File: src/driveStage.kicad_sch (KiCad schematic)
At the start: 73 parts, among them J4 MOD_IN, K1 DIP12-1C90-51L, Q1 BSS138, Q2 SQJA70EP-T1, SW1 204-121ST, SW2 SW_DIP_x03, U1 ADA4898-1YRDZ, U2 ADA4898-1YRDZ, U3 LTC6655BHLS8-4.096#PBF, U4 MAX5719xSD, U5 ADA4898-1YRDZ, U6 LTC6655BHMS8-4.096#PBF, U7 TL082Hx

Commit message: PCB: Correct Y169010R0000T9L Footprint - Add more space between the pin holes and resistor body
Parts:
- R24: footprint Package_TO_SOT_THT:TO-220F-4_Horizontal_TabDown -> kirdy:VPR221_Horizontal
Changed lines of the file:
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@@
       (effects (font (size 1.27 1.27)) (justify right))
     )
-    (property "Footprint" "Package_TO_SOT_THT:TO-220F-4_Horizontal_TabDown" (at 360.68 120.015 0)
+    (property "Footprint" "kirdy:VPR221_Horizontal" (at 360.68 120.015 0)
       (effects (font (size 1.27 1.27)) hide)
     )

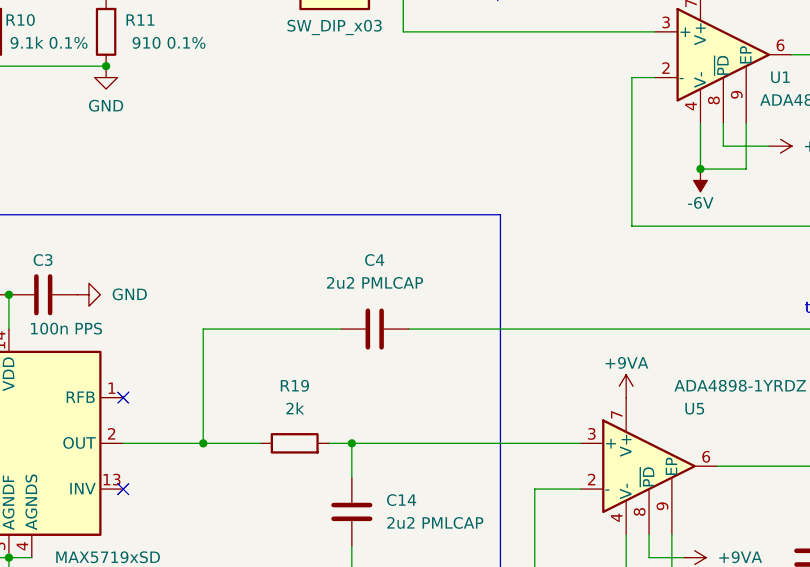
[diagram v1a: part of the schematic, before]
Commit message: sch, pcb: Add TDAC_VFB. Change 2u2 PMLCAP P/N - Connect TDAC voltage output through a RC LPF to MCU PC0(ADC123_IN10) - 2u2 PMLCAP P/N is changed to 16V version instead of 35V for lower cost
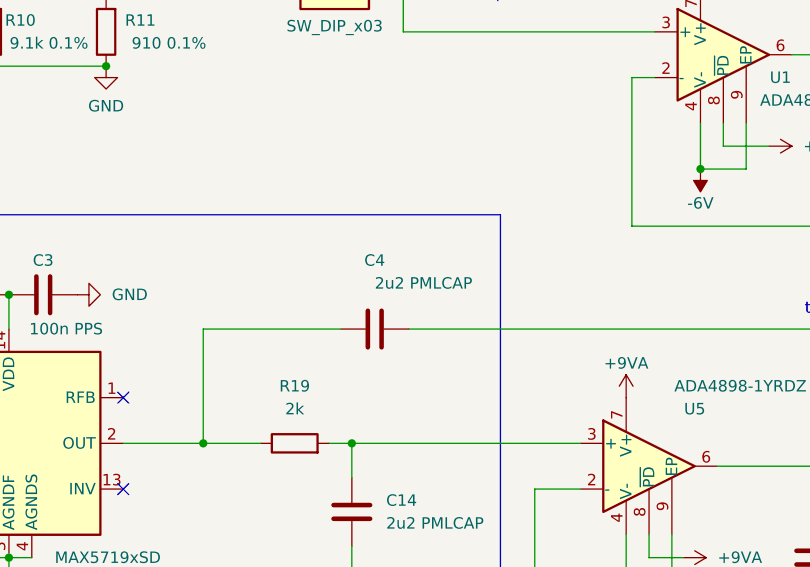
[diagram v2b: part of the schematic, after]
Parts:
- C11, C14, C4: footprint Capacitor_SMD:C_1812_4532Metric -> Capacitor_SMD:C_1210_3225Metric; MFR_PN 35MU225MC14532 -> 16MU225MB23225
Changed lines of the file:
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@@
     )
     (property "Value" "2u2 PMLCAP" (at 154.305 95.25 90)
-      (effects (font (size 1.27 1.27)))
-    )
-    (property "Footprint" "Capacitor_SMD:C_1812_4532Metric" (at 158.115 99.3648 0)
+      (effects (font (size 1.27 1.27)) (justify right))
+    )
+    (property "Footprint" "Capacitor_SMD:C_1210_3225Metric" (at 158.115 99.3648 0)
       (effects (font (size 1.27 1.27)) hide)
     )
@@
       (effects (font (size 1.27 1.27)) hide)
     )
-    (property "MFR_PN" "35MU225MC14532" (at 154.305 100.33 0)
+    (property "MFR_PN" "16MU225MB23225" (at 154.305 100.33 0)
       (effects (font (size 1.27 1.27)) hide)
     )
@@
       (effects (font (size 1.27 1.27)) (justify left))
     )
-    (property "Footprint" "Capacitor_SMD:C_1812_4532Metric" (at 28.2702 113.03 0)
+    (property "Footprint" "Capacitor_SMD:C_1210_3225Metric" (at 28.2702 113.03 0)
       (effects (font (size 1.27 1.27)) hide)
     )
@@
       (effects (font (size 1.27 1.27)) hide)
     )
-    (property "MFR_PN" "35MU225MC14532" (at 27.305 109.22 0)
+    (property "MFR_PN" "16MU225MB23225" (at 27.305 109.22 0)
       (effects (font (size 1.27 1.27)) hide)
     )
@@
       (effects (font (size 1.27 1.27)) (justify left))
     )
-    (property "Footprint" "Capacitor_SMD:C_1812_4532Metric" (at 152.7302 124.46 0)
+    (property "Footprint" "Capacitor_SMD:C_1210_3225Metric" (at 152.7302 124.46 0)
       (effects (font (size 1.27 1.27)) hide)
     )
@@
       (effects (font (size 1.27 1.27)) hide)
     )
-    (property "MFR_PN" "35MU225MC14532" (at 151.765 120.65 0)
-      (effects (font (size 1.27 1.27)) hide)
-    )
+    (property "MFR_PN" "16MU225MB23225" (at 151.765 120.65 0)
+      (effects (font (size 1.27 1.27)) hide)
+    )

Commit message: sch: correct MFR/PNs for BSS138, TLV9001, TPS54620
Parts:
- Q1: MFR_PN BSS138W-TP -> BSS138; MFR_PN_ALT BSS138W-7-F -> (none)
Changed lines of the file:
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@@
       (effects (font (size 1.27 1.27)) (justify left) hide)
     )
-    (property "MFR_PN" "BSS138W-TP" (at 334.01 72.39 0)
+    (property "MFR_PN" "BSS138" (at 334.01 72.39 0)
       (effects (font (size 1.27 1.27)) hide)
     )
-    (property "MFR_PN_ALT" "BSS138W-7-F" (at 334.01 72.39 0)
+    (property "MFR_PN_ALT" "" (at 334.01 72.39 0)
       (effects (font (size 1.27 1.27)) hide)
     )

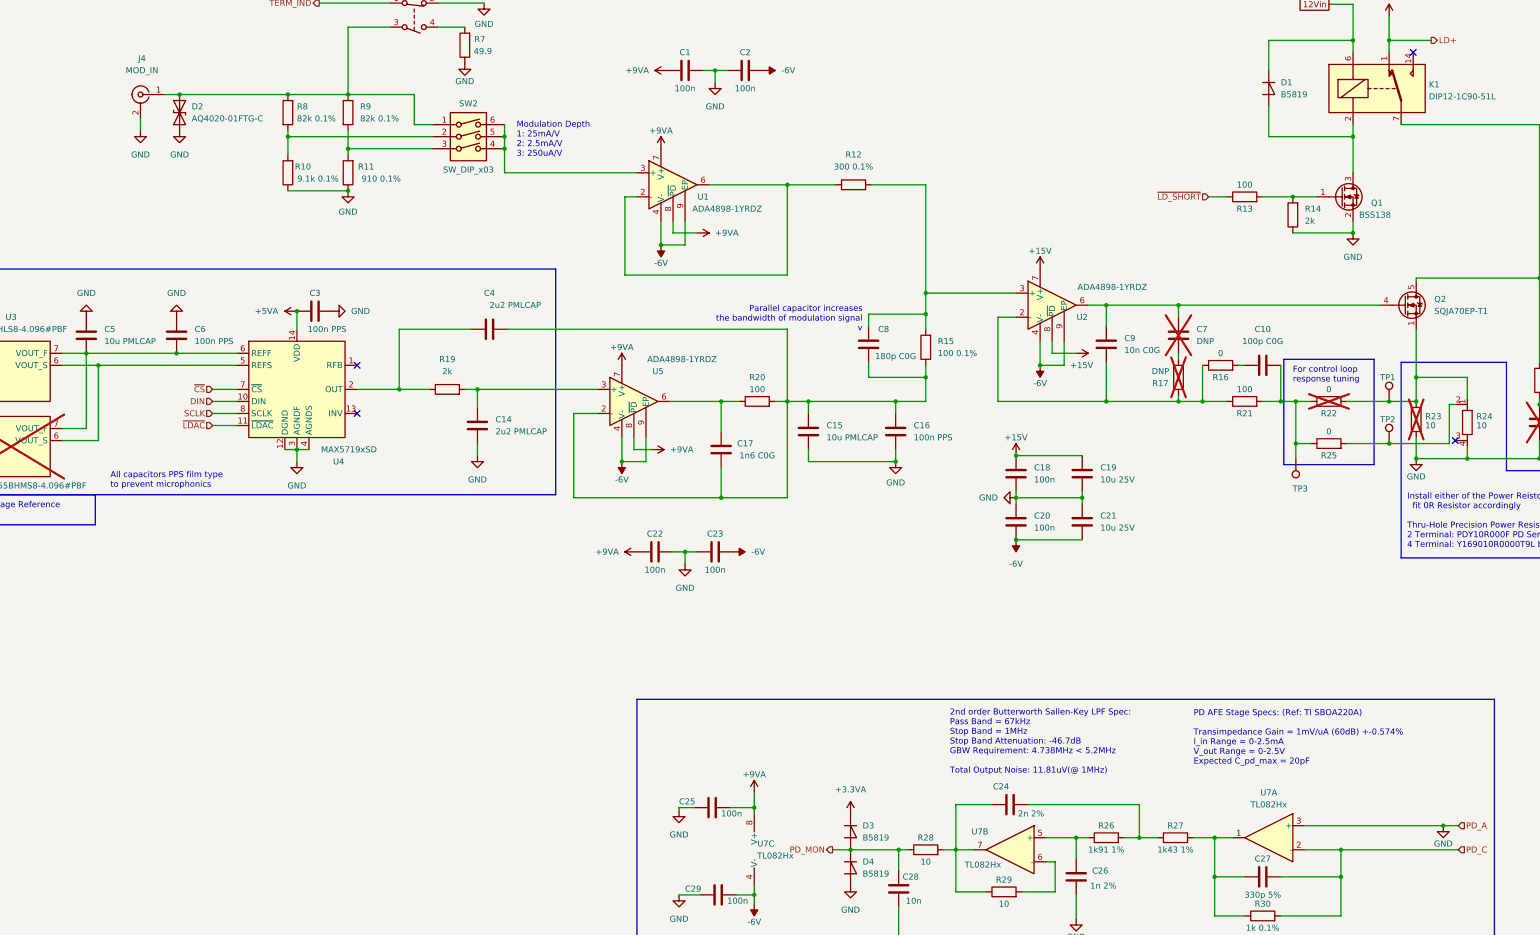
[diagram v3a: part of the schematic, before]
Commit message: Fix issiues from lis, see bug/issiue list in DOC directory
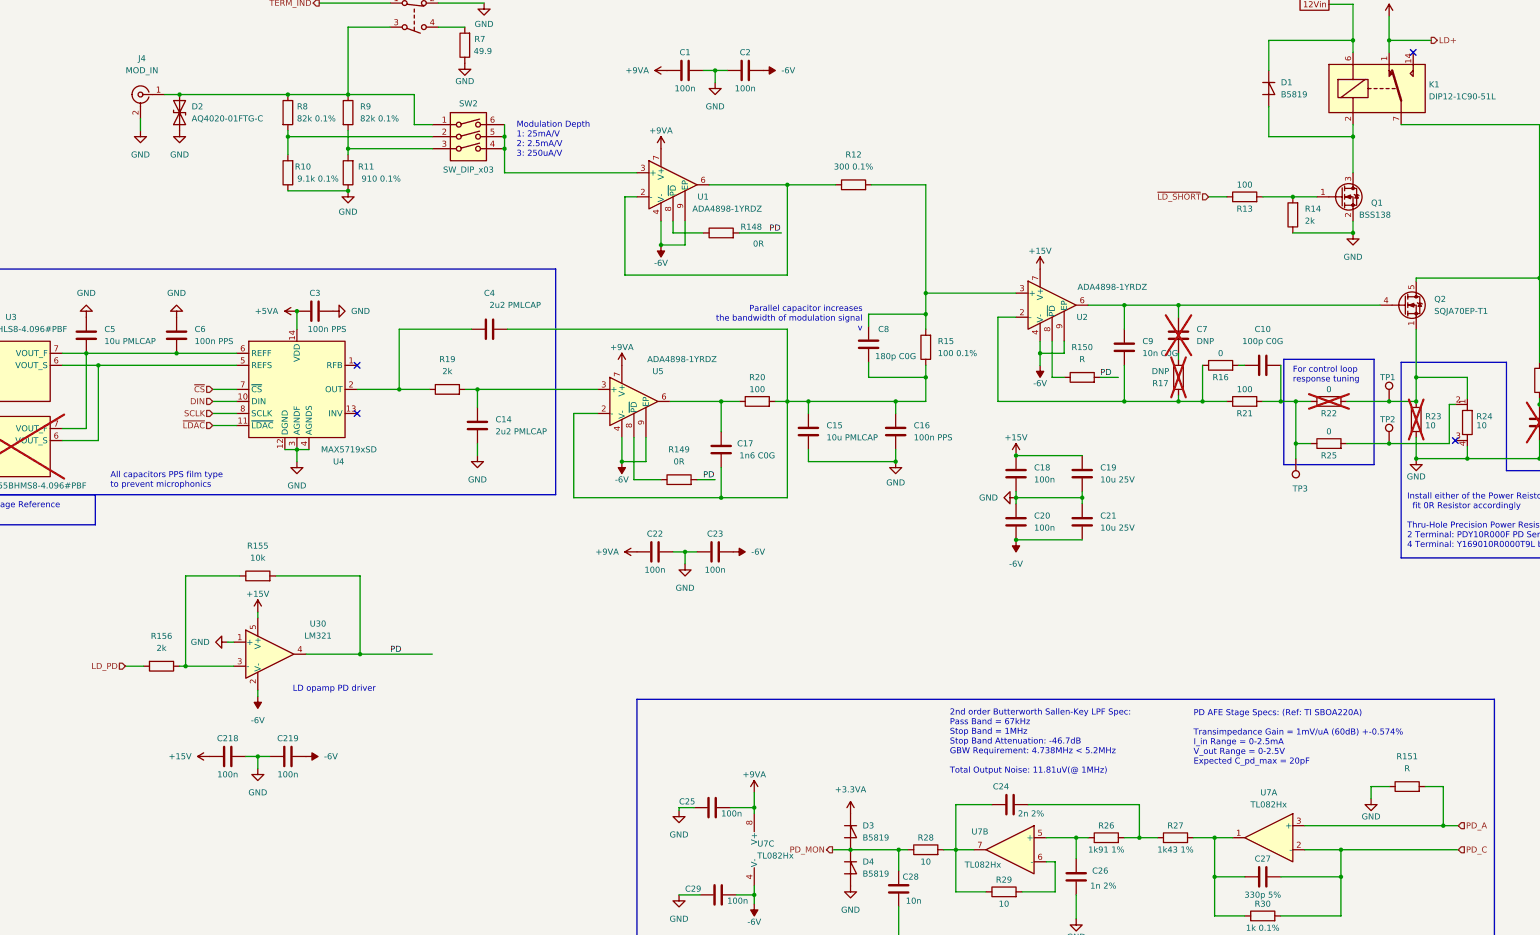
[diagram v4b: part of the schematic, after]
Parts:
- added C218, C219: 100n, Capacitor_SMD:C_0603_1608Metric, symbol Device:C
- added R148, R149: 0R, Resistor_SMD:R_0603_1608Metric, symbol Device:R
- added R150, R151: R, Resistor_SMD:R_0603_1608Metric, symbol Device:R
- added R155: 10k, Resistor_SMD:R_0603_1608Metric, symbol Device:R
- added R156: 2k, Resistor_SMD:R_0603_1608Metric, symbol Device:R
- added U30: LM321, Package_TO_SOT_SMD:SOT-23-5, symbol Amplifier_Operational:LM321
- C13: value 2n2 C0G -> 2n2 C0G
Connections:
- net +15V: now also C218.1, U30.5 (V+); no longer U2.8 (~{PD})
- net +9VA: no longer U1.8 (~{PD}), U5.8 (~{PD})
- net -6V: now also C219.2, U30.2 (V-)
- net GND: now also C218.2, C219.1, R151.1, U30.1 (+); no longer U7.3 (+)
- new net: R155.1, R156.1, U30.3 (-)
- new net: R148.1, U1.8 (~{PD})
- new net: R150.1, U2.8 (~{PD})
- new net: R149.1, U5.8 (~{PD})
- new net LD_PD: R156.2
- new net PD: R148.2, R149.2, R150.2, R155.2, U30.4
- new net PD_A: R151.2, U7.3 (+)
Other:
- note added: "LD opamp PD driver"
- moved on the sheet: C9
